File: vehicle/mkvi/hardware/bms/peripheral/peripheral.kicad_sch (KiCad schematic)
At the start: 10 parts, among them Q1 NSS1C201MZ4, U1 MCP6001T-I-LT, U2 ADBMS1818

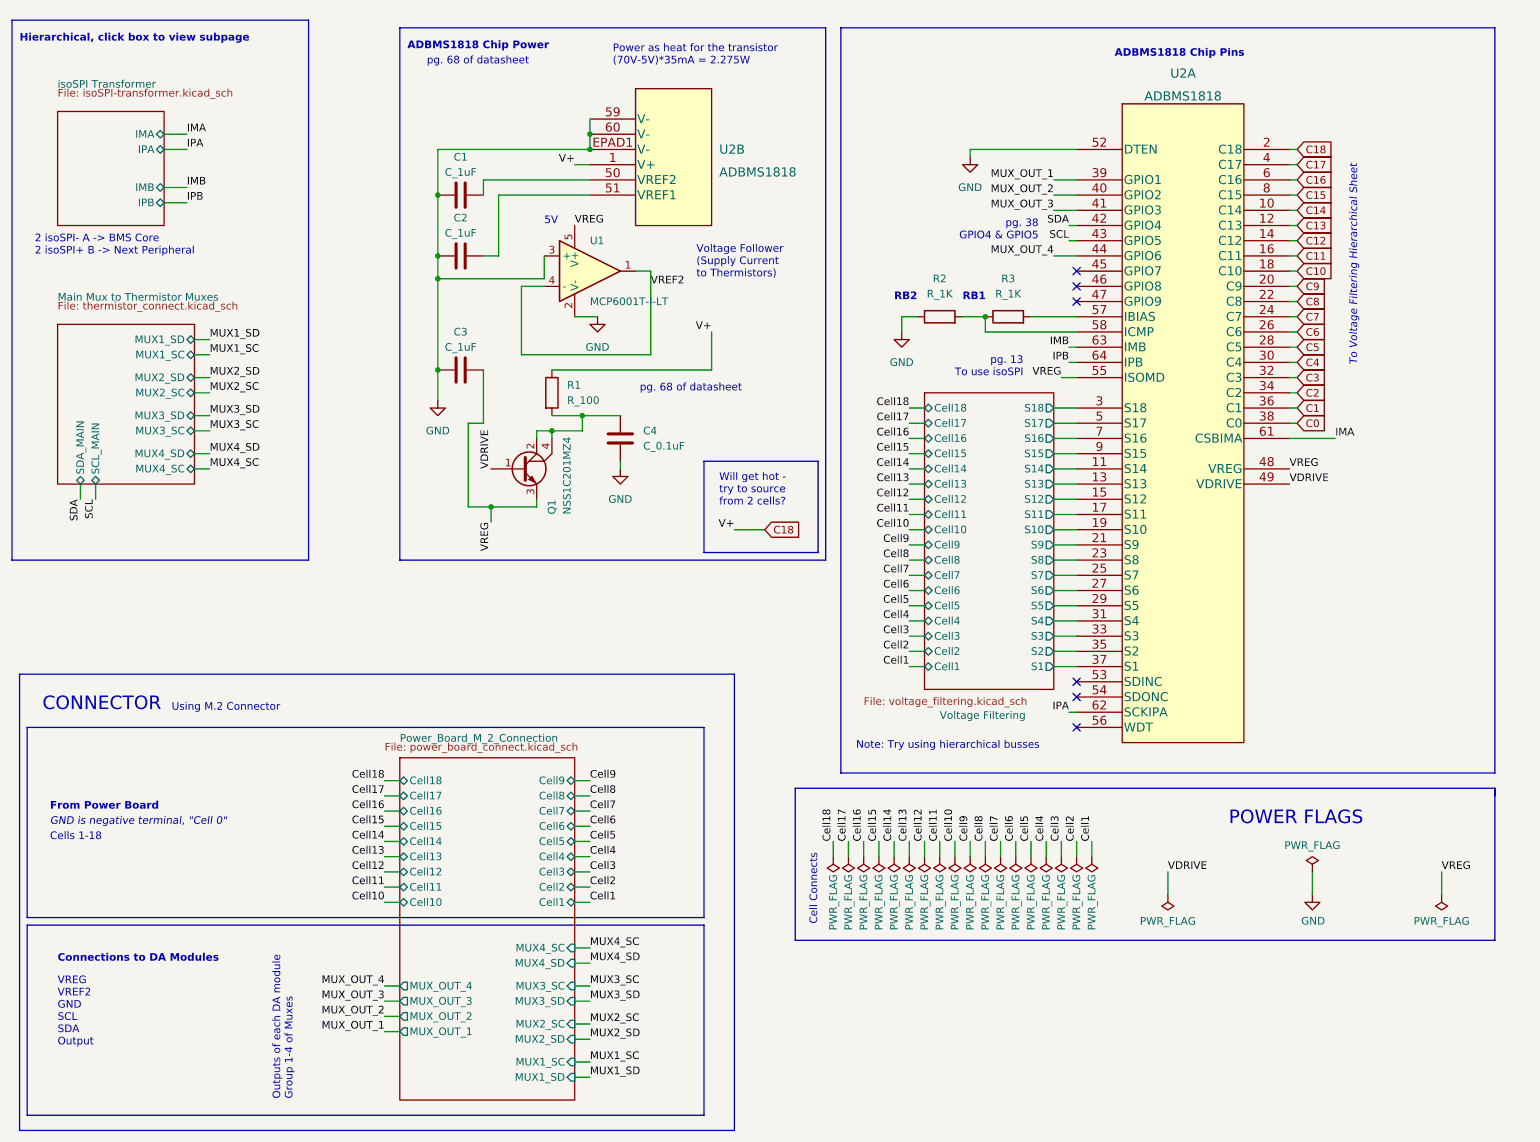
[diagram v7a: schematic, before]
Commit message: Clean schematic for peripheral and DA modules
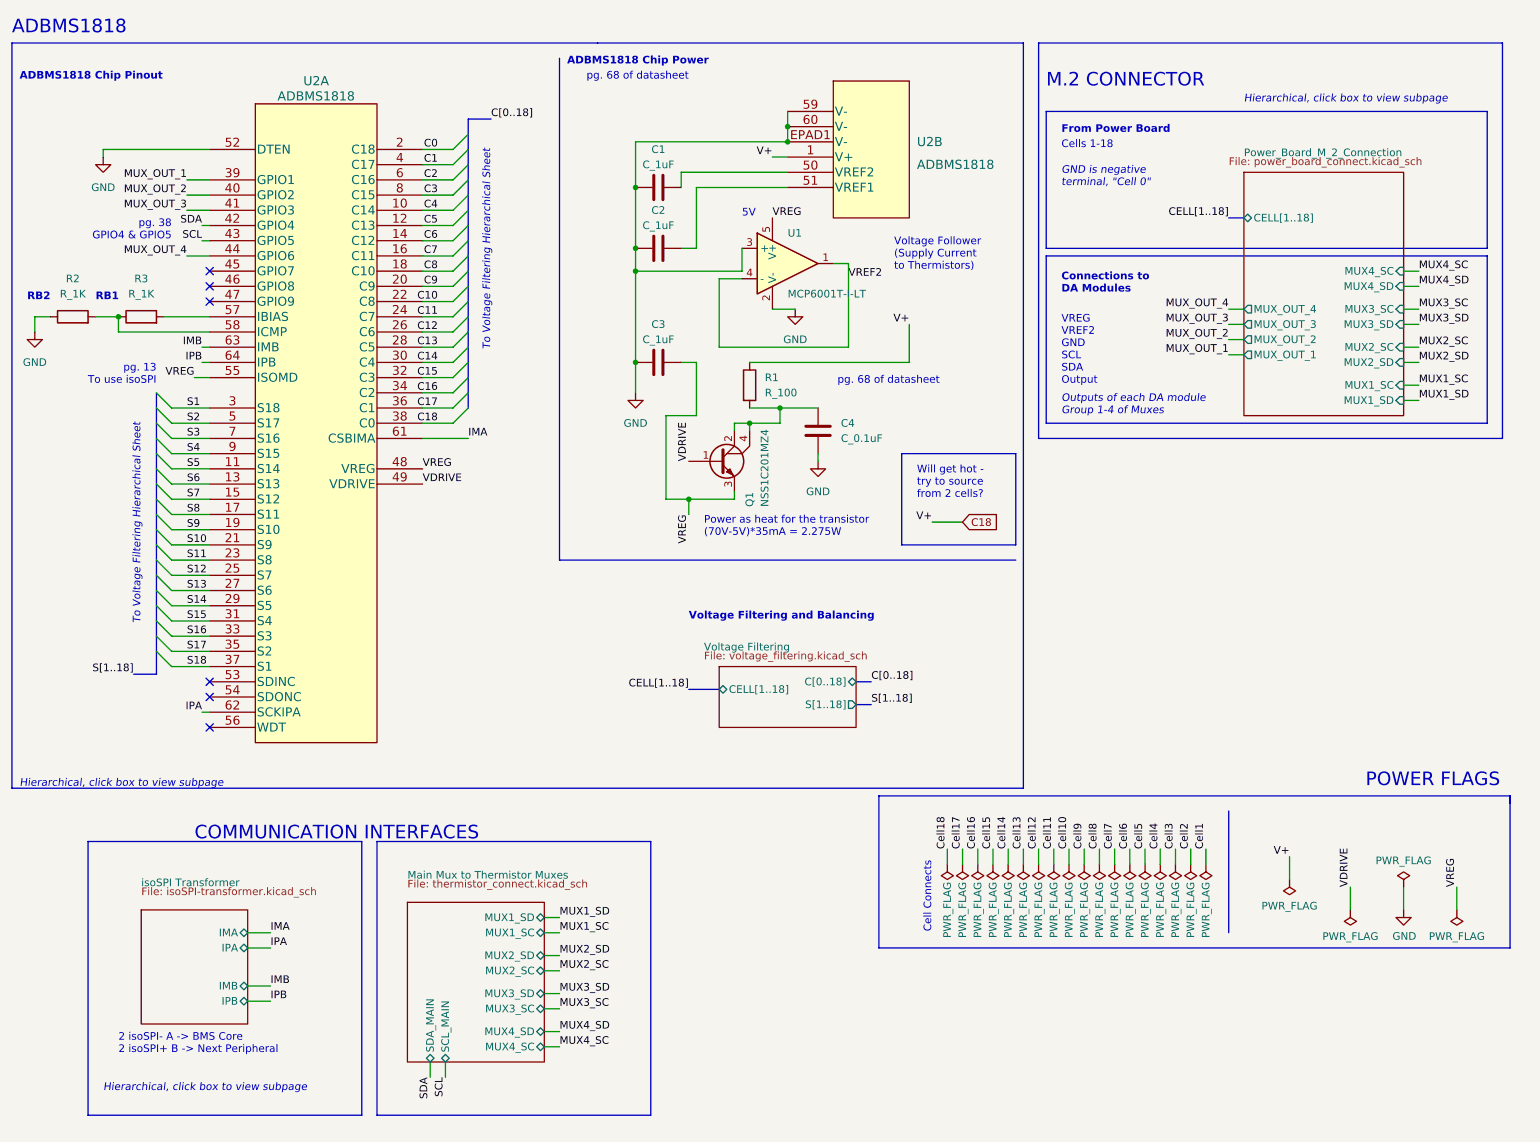
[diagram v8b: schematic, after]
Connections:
- net C0: now also U2.2 (C18); no longer U2.38 (C0)
- net C1: now also U2.4 (C17); no longer U2.36 (C1)
- net C10: now also U2.22 (C8); no longer U2.18 (C10)
- net C11: now also U2.24 (C7); no longer U2.16 (C11)
- net C12: now also U2.26 (C6); no longer U2.14 (C12)
- net C13: now also U2.28 (C5); no longer U2.12 (C13)
- net C14: now also U2.30 (C4); no longer U2.10 (C14)
- net C15: now also U2.32 (C3); no longer U2.8 (C15)
- net C16: now also U2.34 (C2); no longer U2.6 (C16)
- net C17: now also U2.36 (C1); no longer U2.4 (C17)
- net C18: now also U2.38 (C0); no longer U2.2 (C18)
- net C2: now also U2.6 (C16); no longer U2.34 (C2)
- net C3: now also U2.8 (C15); no longer U2.32 (C3)
- net C4: now also U2.10 (C14); no longer U2.30 (C4)
- net C5: now also U2.12 (C13); no longer U2.28 (C5)
- net C6: now also U2.14 (C12); no longer U2.26 (C6)
- net C7: now also U2.16 (C11); no longer U2.24 (C7)
- net C8: now also U2.18 (C10); no longer U2.22 (C8)
- net Voltage Filtering/S1 renamed S18
- net Voltage Filtering/S10 renamed S9
- net Voltage Filtering/S11 renamed S8
- net Voltage Filtering/S12 renamed S7
- net Voltage Filtering/S13 renamed S6
- net Voltage Filtering/S14 renamed S5
- net Voltage Filtering/S15 renamed S4
- net Voltage Filtering/S16 renamed S3
- net Voltage Filtering/S17 renamed S2
- net Voltage Filtering/S18 renamed S1
- net Voltage Filtering/S2 renamed S17
- net Voltage Filtering/S3 renamed S16
- net Voltage Filtering/S4 renamed S15
- net Voltage Filtering/S5 renamed S14
- net Voltage Filtering/S6 renamed S13
- net Voltage Filtering/S7 renamed S12
- net Voltage Filtering/S8 renamed S11
- net Voltage Filtering/S9 renamed S10
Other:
- sheet Power_Board_M_2_Connection ports: added CELL[1..18]; removed Cell1, Cell10, Cell11, Cell12, Cell13, Cell14, Cell15, Cell16, Cell17, Cell18, Cell2, Cell3, Cell4, Cell5, Cell6, Cell7, Cell8, Cell9
- sheet Voltage Filtering ports: added CELL[1..18], C[0..18], S[1..18]; removed Cell1, Cell10, Cell11, Cell12, Cell13, Cell14, Cell15, Cell16, Cell17, Cell18, Cell2, Cell3, Cell4, Cell5, Cell6, Cell7, Cell8, Cell9, S1, S10, S11, S12, S13, S14, S15, S16, S17, S18, S2, S3, S4, S5, S6, S7, S8, S9
- note added: "ADBMS1818"
- note added: "ADBMS1818 Chip Pinout"
- note added: "COMMUNICATION INTERFACES"
- note added: "M.2 CONNECTOR"
- note added: "Voltage Filtering and Balancing"
- note removed: "ADBMS1818 Chip Pins"
- note removed: "CONNECTOR"
- note removed: "Note: Try using hierarchical busses"
- note removed: "Using M.2 Connector"
- moved on the sheet: C1, C2, C3, C4, Q1, R1, R2, R3, U1, U2A, U2B
